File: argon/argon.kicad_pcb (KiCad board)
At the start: 2 copper layers, 60 x 60 mm, 77 parts, among them J1 USB, J2 V3V3-GND, J3 V3V3-GND, J4 V3V3-GND, J5 V3V3-GND, J6 V3V3-GND, J7 V3V3-GND, U1 LMC555xM, U2 AMS1117-3.3, U3 93LCxxA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

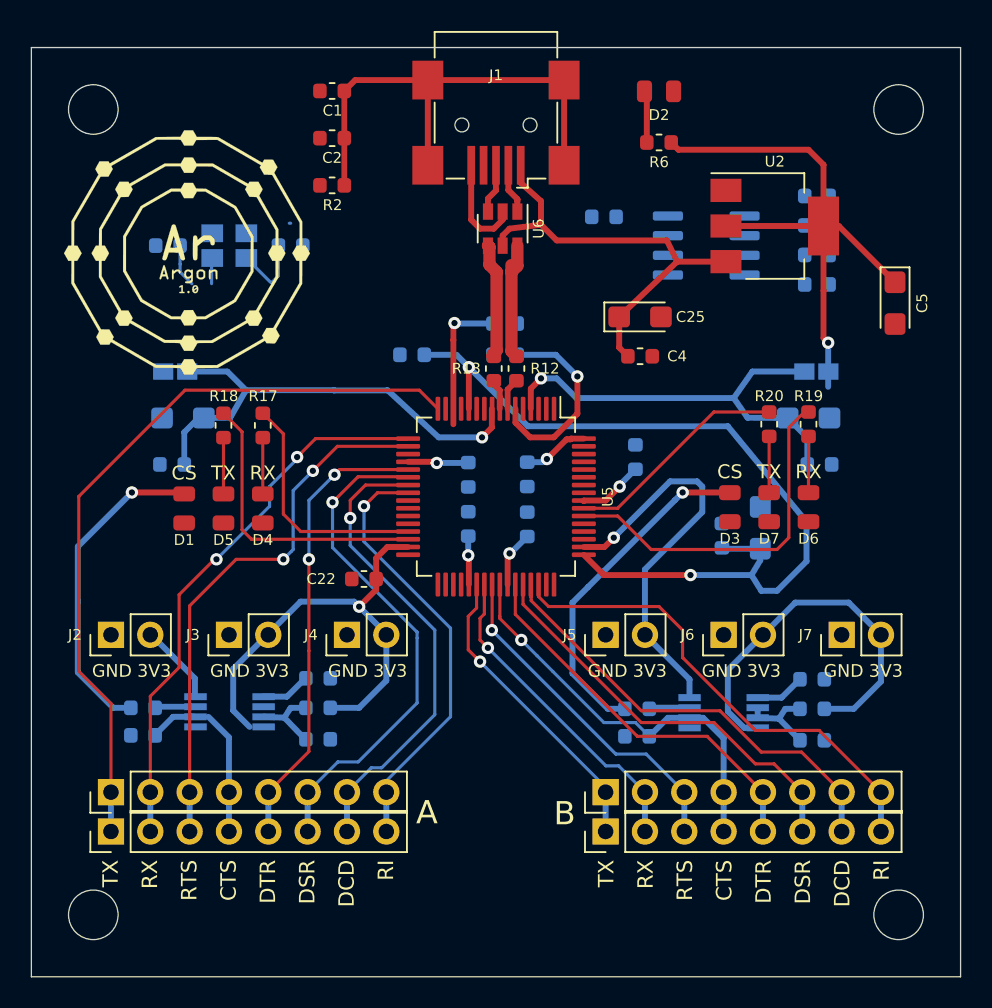
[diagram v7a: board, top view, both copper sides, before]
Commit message: EEPROM routing
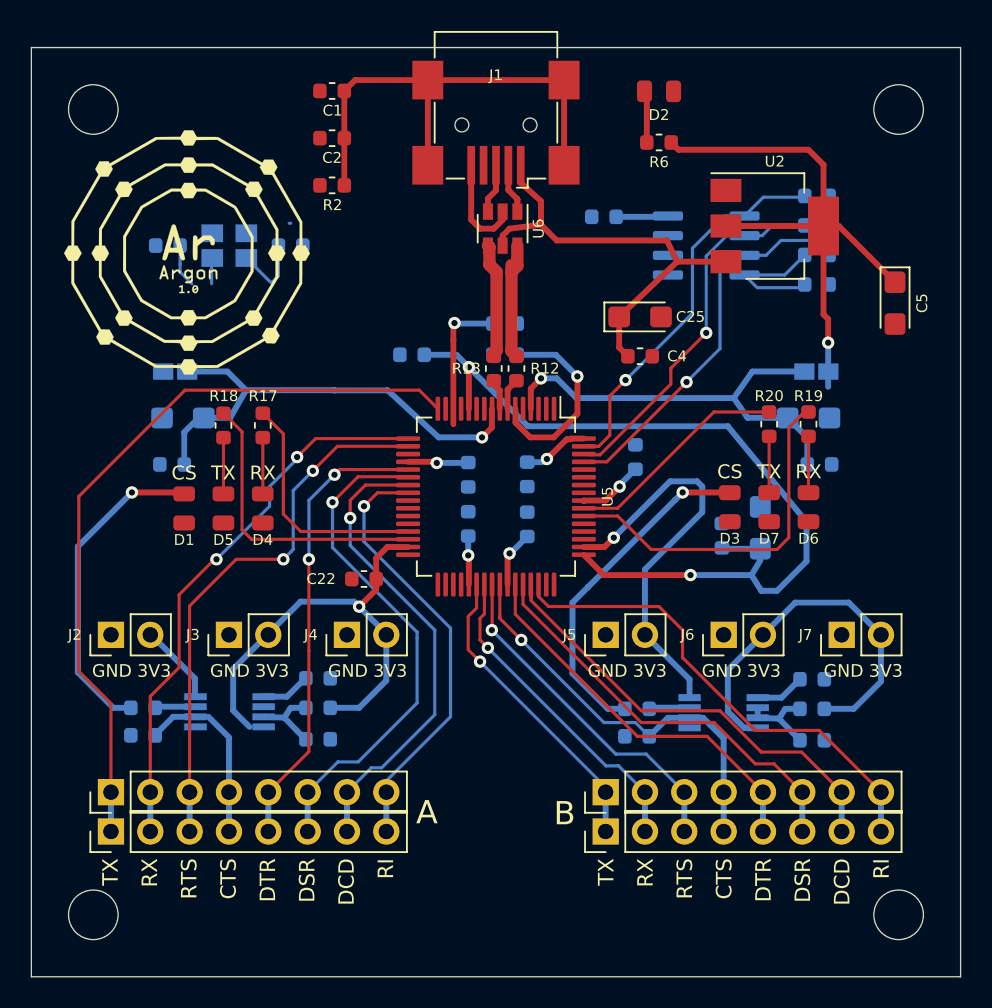
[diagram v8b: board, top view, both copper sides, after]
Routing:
- net Net-(R8-Pad1): track 0.00 -> 25.3 mm, vias 0 -> 1
- net Net-(R9-Pad1): track 0.00 -> 24.9 mm, vias 0 -> 1
- net Net-(R7-Pad1): track 0.00 -> 24.3 mm, vias 0 -> 1
- net Net-(R5-Pad1): track 0.00 -> 8.89 mm
- net V3V3: track 136.6 -> 140.0 mm
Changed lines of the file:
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@@
     (thickness 1.6)
     (drawings 53)
-    (tracks 416)
+    (tracks 465)
     (zones 0)
     (modules 77)
@@
   )
   (setup
-    (last_trace_width 0.381)
+    (last_trace_width 0.2032)
     (user_trace_width 0.2032)
     (user_trace_width 0.3)
@@
     (effects (font (size 0.82 0.82) (thickness 0.15)) (justify right))
   )
-  (gr_text "RTS\n" (at 162.198 132.444 90) (layer F.SilkS)
+  (gr_text "RTS\n" (at 162.198 132.344 90) (layer F.SilkS)
     (effects (font (size 1 1) (thickness 0.2)) (justify right))
   )
-  (gr_text RX (at 159.658 132.444 90) (layer F.SilkS)
+  (gr_text RX (at 159.658 132.344 90) (layer F.SilkS)
     (effects (font (size 1 1) (thickness 0.2)) (justify right))
   )
-  (gr_text DTR (at 167.278 132.444 90) (layer F.SilkS)
+  (gr_text DTR (at 167.278 132.344 90) (layer F.SilkS)
     (effects (font (size 1 1) (thickness 0.2)) (justify right))
   )
-  (gr_text CTS (at 164.738 132.444 90) (layer F.SilkS)
+  (gr_text CTS (at 164.738 132.344 90) (layer F.SilkS)
     (effects (font (size 1 1) (thickness 0.2)) (justify right))
   )
-  (gr_text TX (at 157.118 132.444 90) (layer F.SilkS)
+  (gr_text TX (at 157.118 132.344 90) (layer F.SilkS)
     (effects (font (size 1 1) (thickness 0.2)) (justify right))
   )
-  (gr_text "RI\n" (at 174.898 132.444 90) (layer F.SilkS)
+  (gr_text "RI\n" (at 174.898 132.344 90) (layer F.SilkS)
     (effects (font (size 1 1) (thickness 0.2)) (justify right))
   )
-  (gr_text DSR (at 169.818 132.444 90) (layer F.SilkS)
+  (gr_text DSR (at 169.818 132.344 90) (layer F.SilkS)
     (effects (font (size 1 1) (thickness 0.2)) (justify right))
   )
-  (gr_text DCD (at 172.358 132.444 90) (layer F.SilkS)
+  (gr_text DCD (at 172.358 132.344 90) (layer F.SilkS)
     (effects (font (size 1 1) (thickness 0.2)) (justify right))
   )
-  (gr_text DCD (at 140.354 132.444 90) (layer F.SilkS)
+  (gr_text DCD (at 140.354 132.344 90) (layer F.SilkS)
     (effects (font (size 1 1) (thickness 0.2)) (justify right))
   )
-  (gr_text "RI\n" (at 142.894 132.444 90) (layer F.SilkS)
+  (gr_text "RI\n" (at 142.894 132.344 90) (layer F.SilkS)
     (effects (font (size 1 1) (thickness 0.2)) (justify right))
   )
-  (gr_text DSR (at 137.814 132.444 90) (layer F.SilkS)
+  (gr_text DSR (at 137.814 132.344 90) (layer F.SilkS)
     (effects (font (size 1 1) (thickness 0.2)) (justify right))
   )
-  (gr_text DTR (at 135.274 132.444 90) (layer F.SilkS)
+  (gr_text DTR (at 135.274 132.344 90) (layer F.SilkS)
     (effects (font (size 1 1) (thickness 0.2)) (justify right))
   )
-  (gr_text CTS (at 132.734 132.444 90) (layer F.SilkS)
+  (gr_text CTS (at 132.734 132.344 90) (layer F.SilkS)
     (effects (font (size 1 1) (thickness 0.2)) (justify right))
   )
-  (gr_text "RTS\n" (at 130.194 132.444 90) (layer F.SilkS)
+  (gr_text "RTS\n" (at 130.194 132.344 90) (layer F.SilkS)
     (effects (font (size 1 1) (thickness 0.2)) (justify right))
   )
-  (gr_text RX (at 127.654 132.444 90) (layer F.SilkS)
+  (gr_text RX (at 127.654 132.344 90) (layer F.SilkS)
     (effects (font (size 1 1) (thickness 0.2)) (justify right))
   )
@@
     (arrow2b (pts (xy 111.411 99.6) (xy 111.997421 100.726504)))
   )
-  (gr_text TX (at 125.114 132.444 90) (layer F.SilkS)
+  (gr_text TX (at 125.114 132.344 90) (layer F.SilkS)
     (effects (font (size 1 1) (thickness 0.2)) (justify right))
   )
@@
   (segment (start 150 87.6) (end 150 89.231) (width 0.381) (layer F.Cu) (net 6))
   (segment (start 149.4815 89.7495) (end 149.4815 90.594) (width 0.381) (layer F.Cu) (net 6))
+  (segment (start 166.051 92.147) (end 167.187 92.147) (width 0.2032) (layer B.Cu) (net 7))
+  (segment (start 167.846 91.488) (end 169.938 91.488) (width 0.2032) (layer B.Cu) (net 7))
+  (segment (start 167.187 92.147) (end 167.846 91.488) (width 0.2032) (layer B.Cu) (net 7))
+  (segment (start 165.663 92.147) (end 166.051 92.147) (width 0.2032) (layer B.Cu) (net 7))
+  (segment (start 166.051 92.147) (end 164.901 92.147) (width 0.2032) (layer B.Cu) (net 7))
+  (segment (start 164.901 92.147) (end 163.576 93.472) (width 0.2032) (layer B.Cu) (net 7))
+  (via (at 163.576 98.425) (size 0.8) (drill 0.4) (layers F.Cu B.Cu) (net 7))
+  (segment (start 163.576 93.472) (end 163.576 98.425) (width 0.2032) (layer B.Cu) (net 7))
+  (segment (start 156.034 106.25) (end 155.675 106.25) (width 0.2032) (layer F.Cu) (net 7))
+  (segment (start 163.576 98.425) (end 161.29 100.711) (width 0.2032) (layer F.Cu) (net 7))
+  (segment (start 161.29 100.711) (end 161.29 101.727) (width 0.2032) (layer F.Cu) (net 7))
+  (segment (start 161.29 101.727) (end 156.718 106.299) (width 0.2032) (layer F.Cu) (net 7))
+  (segment (start 156.718 106.299) (end 156.083 106.299) (width 0.2032) (layer F.Cu) (net 7))
+  (segment (start 156.083 106.299) (end 156.034 106.25) (width 0.2032) (layer F.Cu) (net 7))
+  (segment (start 166.051 90.877) (end 167.266 89.662) (width 0.2032) (layer B.Cu) (net 8))
+  (segment (start 169.859 89.662) (end 169.938 89.583) (width 0.2032) (layer B.Cu) (net 8))
+  (segment (start 167.266 89.662) (end 169.859 89.662) (width 0.2032) (layer B.Cu) (net 8))
+  (segment (start 166.051 90.877) (end 164.774 90.877) (width 0.2032) (layer B.Cu) (net 8))
+  (segment (start 164.774 90.877) (end 162.687 92.964) (width 0.2032) (layer B.Cu) (net 8))
+  (segment (start 162.687 92.964) (end 162.687 97.028) (width 0.2032) (layer B.Cu) (net 8))
+  (segment (start 162.687 97.028) (end 162.687 97.155) (width 0.2032) (layer B.Cu) (net 8))
+  (via (at 158.369 101.473) (size 0.8) (drill 0.4) (layers F.Cu B.Cu) (net 8))
+  (segment (start 162.687 97.155) (end 158.369 101.473) (width 0.2032) (layer B.Cu) (net 8))
+  (segment (start 158.369 101.473) (end 157.353 102.489) (width 0.2032) (layer F.Cu) (net 8))
+  (segment (start 155.675 105.75) (end 156.632 105.75) (width 0.2032) (layer F.Cu) (net 8))
+  (segment (start 157.353 105.029) (end 157.353 102.489) (width 0.2032) (layer F.Cu) (net 8))
+  (segment (start 156.632 105.75) (end 157.353 105.029) (width 0.2032) (layer F.Cu) (net 8))
   (segment (start 151.3715 99.838) (end 153.8605 99.838) (width 0.381) (layer B.Cu) (net 9))
   (via (at 155.2575 101.235) (size 0.8) (drill 0.4) (layers F.Cu B.Cu) (net 9))
@@
   (segment (start 172.138 91.524) (end 175.768 95.154) (width 0.381) (layer F.Cu) (net 18))
   (segment (start 171.15 91.524) (end 172.138 91.524) (width 0.381) (layer F.Cu) (net 18))
-  (segment (start 171.15 91.524) (end 171.15 95.696) (width 0.381) (layer F.Cu) (net 18))
-  (segment (start 171.15 95.696) (end 171.15 98.76) (width 0.381) (layer F.Cu) (net 18))
   (via (at 171.45 99.06) (size 0.8) (drill 0.4) (layers F.Cu B.Cu) (net 18))
-  (segment (start 171.15 98.76) (end 171.45 99.06) (width 0.381) (layer F.Cu) (net 18))
   (segment (start 171.45 100.905918) (end 171.464082 100.92) (width 0.381) (layer B.Cu) (net 18))
   (segment (start 171.45 99.06) (end 171.45 101.905918) (width 0.381) (layer B.Cu) (net 18))
@@
   (segment (start 142.2655 114.316) (end 142.2655 115.0017) (width 0.381) (layer F.Cu) (net 18))
   (segment (start 141.1651 116.1021) (end 142.9195 117.8565) (width 0.381) (layer B.Cu) (net 18))
+  (segment (start 171.45 97.536) (end 171.45 99.06) (width 0.381) (layer F.Cu) (net 18))
+  (segment (start 171.15 91.524) (end 171.15 97.236) (width 0.381) (layer F.Cu) (net 18))
+  (segment (start 171.15 97.236) (end 171.45 97.536) (width 0.381) (layer F.Cu) (net 18))
+  (segment (start 161.046 90.932) (end 161.101 90.877) (width 0.381) (layer B.Cu) (net 18))
+  (segment (start 157.7595 90.932) (end 161.046 90.932) (width 0.381) (layer B.Cu) (net 18))
   (segment (start 148.25 103.325) (end 148.25 100.641) (width 0.381) (layer F.Cu) (net 19))
   (via (at 148.25 100.641) (size 0.8) (drill 0.4) (layers F.Cu B.Cu) (net 19))
@@
   (segment (start 132.76 128.08) (end 132.76 130.62) (width 0.381) (layer B.Cu) (net 32))
   (segment (start 130.5595 122.5635) (end 128.03 122.5635) (width 0.381) (layer B.Cu) (net 33))
+  (segment (start 169.89 95.25) (end 169.938 95.298) (width 0.381) (layer B.Cu) (net 34))
+  (segment (start 168.644 94.687) (end 166.051 94.687) (width 0.2032) (layer B.Cu) (net 34))
+  (segment (start 169.938 93.393) (end 168.644 94.687) (width 0.2032) (layer B.Cu) (net 34))
+  (segment (start 166.051 94.687) (end 166.868 95.504) (width 0.2032) (layer B.Cu) (net 34))
+  (segment (start 169.732 95.504) (end 169.938 95.298) (width 0.2032) (layer B.Cu) (net 34))
+  (segment (start 166.868 95.504) (end 169.732 95.504) (width 0.2032) (layer B.Cu) (net 34))
+  (segment (start 169.938 93.393) (end 169.938 93.484) (width 0.2032) (layer B.Cu) (net 34))
+  (segment (start 166.051 93.417) (end 167.441 93.417) (width 0.2032) (layer B.Cu) (net 35))
+  (segment (start 167.441 93.417) (end 168.402 92.456) (width 0.2032) (layer B.Cu) (net 35))
+  (segment (start 170.576 92.456) (end 171.513 93.393) (width 0.2032) (layer B.Cu) (net 35))
+  (segment (start 168.402 92.456) (end 170.576 92.456) (width 0.2032) (layer B.Cu) (net 35))
+  (segment (start 157.156 106.75) (end 155.675 106.75) (width 0.2032) (layer F.Cu) (net 35))
+  (segment (start 157.734 106.172) (end 157.156 106.75) (width 0.2032) (layer F.Cu) (net 35))
+  (segment (start 157.734 106.172) (end 162.306 101.6) (width 0.2032) (layer F.Cu) (net 35))
+  (via (at 162.306 101.6) (size 0.8) (drill 0.4) (layers F.Cu B.Cu) (net 35))
+  (segment (start 163.068 100.838) (end 162.306 101.6) (width 0.2032) (layer B.Cu) (net 35))
+  (segment (start 166.051 93.417) (end 165.155 93.417) (width 0.2032) (layer B.Cu) (net 35))
+  (segment (start 165.155 93.417) (end 164.465 94.107) (width 0.2032) (layer B.Cu) (net 35))
+  (segment (start 164.465 99.441) (end 163.068 100.838) (width 0.2032) (layer B.Cu) (net 35))
+  (segment (start 164.465 94.107) (end 164.465 99.441) (width 0.2032) (layer B.Cu) (net 35))
   (segment (start 164.7 124.605498) (end 164.7 128.08) (width 0.381) (layer B.Cu) (net 36))
   (segment (start 163.371502 123.277) (end 164.7 124.605498) (width 0.381) (layer B.Cu) (net 36))
